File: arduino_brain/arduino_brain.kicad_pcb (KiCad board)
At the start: 2 copper layers, 624 parts, among them J1 Conn_01x08_Male, J2 Conn_01x10_Male, J3 Conn_01x08_Male, J4 Conn_01x06_Male, Q1 2N3904, Q10 2N3904, Q11 2N3906, Q12 STP36NF06L, Q2 TIP120, Q3 2N3904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

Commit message: Updated PCB
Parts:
- added R51: CFR16-10k, Resistor_THT:R_Axial_DIN0204_L3.6mm_D1.6mm_P2.54mm_Vertical, F.Cu at (10.2, -15.2)
- added U2: CRE1S2412SC, Converter_DCDC:Converter_DCDC_muRata_CRE1xxxxxxSC_THT, F.Cu at (0.00, -15.2)
- moved R20 48.2 mm to (20.3, 40.6), turned to 0 degrees
- moved R17 45.0 mm to (20.3, 43.2), turned to 0 degrees
- moved R10 10.5 mm to (33.0, 83.8)
- moved R14 10.5 mm to (35.6, 83.8)
- moved R6 5.08 mm to (27.9, 73.7)
- moved R4 3.59 mm to (30.5, 73.7), turned to 0 degrees
- moved R5 2.54 mm to (27.9, 71.1)
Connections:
- J3 pad 6: COMMODO_GND -> Net-(A1-Pad6)
- R17 pad 1: A1_A2 -> A1_D1
- R20 pad 1: A1_A3 -> A1_D0
- R4 pad 2: A1_D0 -> A1_A2

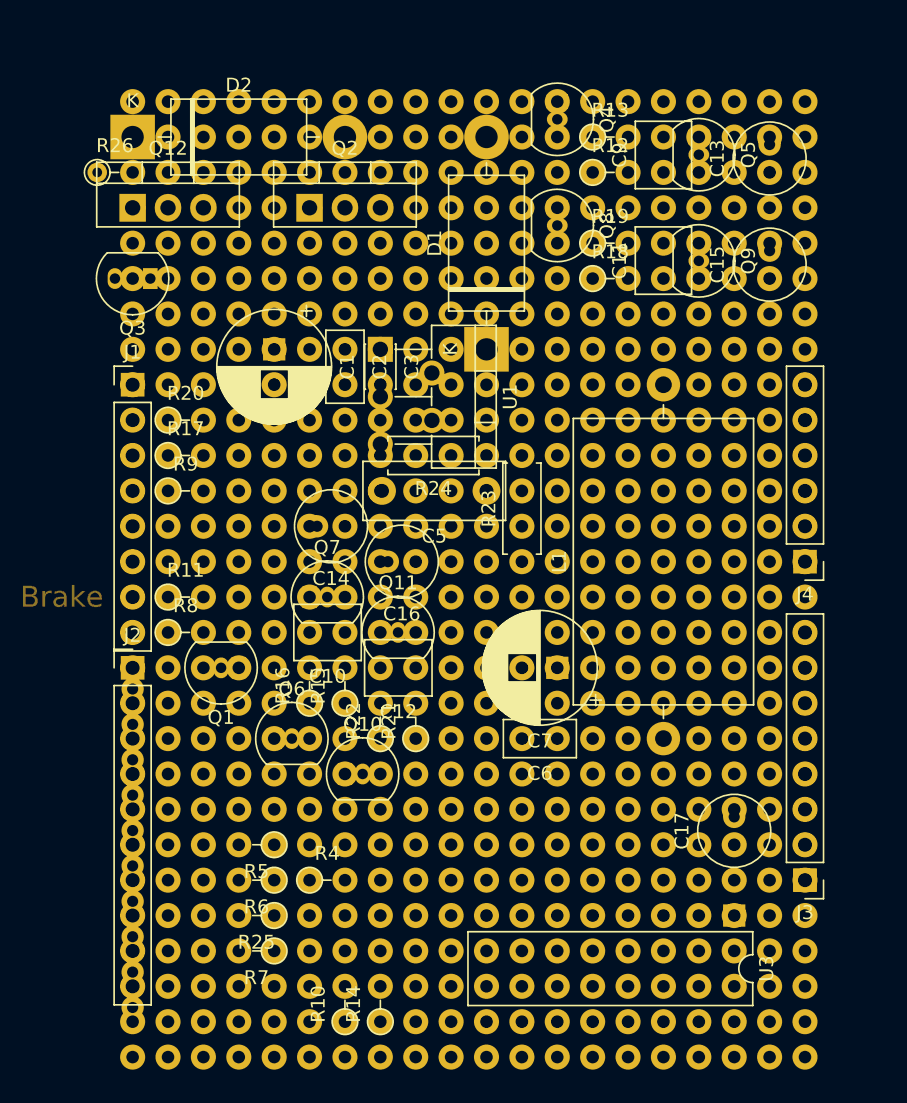
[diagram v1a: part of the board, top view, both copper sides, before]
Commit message: Started routes on PCzb, locking components already placed
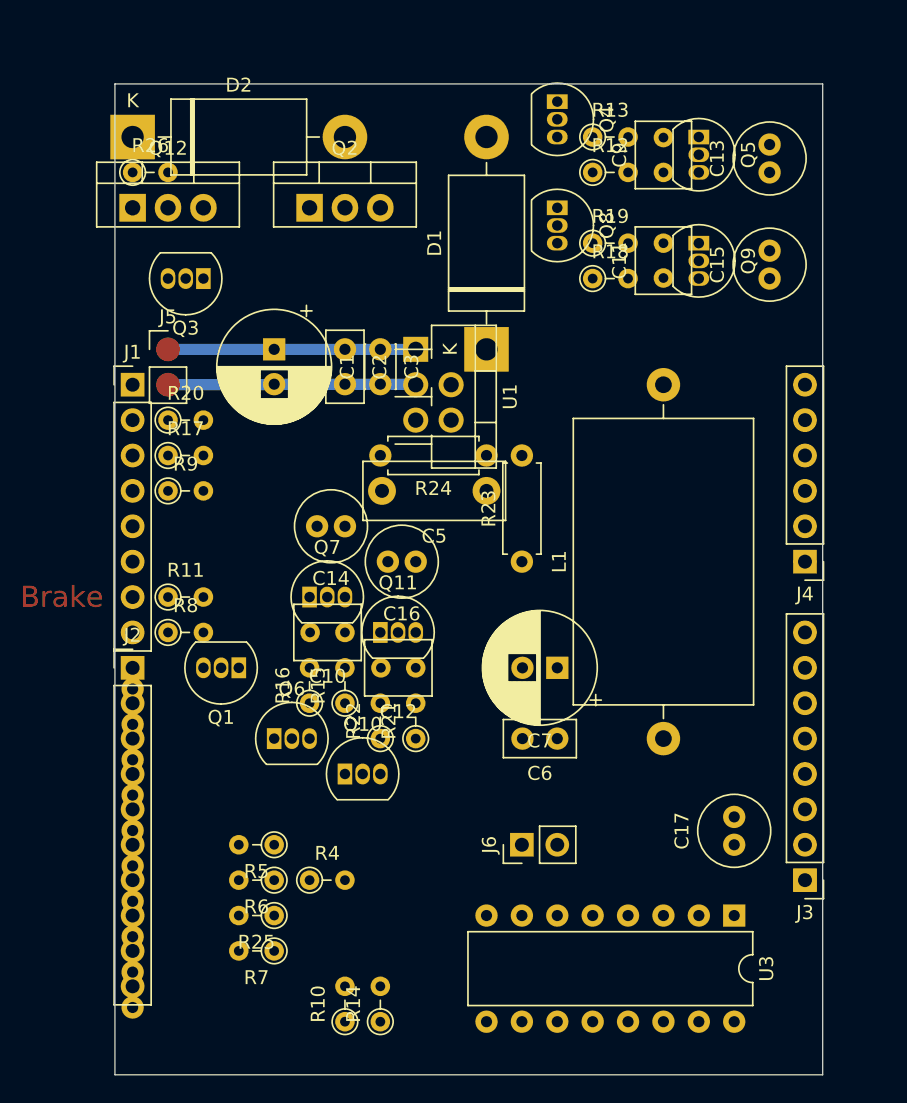
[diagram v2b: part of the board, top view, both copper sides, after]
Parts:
- removed REF** (x560): Pin_D0.9mm_L10.0mm_W2.4mm_FlatFork, Connector_Pin:Pin_D0.9mm_L10.0mm_W2.4mm_FlatFork
- added J5: 12V cable from regulator, Connector_PinHeader_2.54mm:PinHeader_1x02_P2.54mm_Vertical, F.Cu at (20.3, 35.6)
- added J6: 7.5V cables x2 to Arduino power jacks, Connector_PinHeader_2.54mm:PinHeader_1x02_P2.54mm_Vertical, F.Cu at (45.7, 71.1)
- moved Q3 3.81 mm to (22.9, 30.5)
- moved R26 2.54 mm to (17.8, 22.9)
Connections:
- A1 pad 6: Net-(A1-Pad6) -> COMMODO_GND
- J3 pad 6: Net-(A1-Pad6) -> COMMODO_GND
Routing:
- net COMMODO_GND: track 0.00 -> 17.8 mm
- net BEAM_+12V: track 0.00 -> 17.8 mm
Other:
- board outline added: 50.8 x 71.1 mm
- net class Rustic added: clearance 0.35, trace_width 0.8, via_dia 1.91, via_drill 0.4

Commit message: Finsihed solder routes on PCB
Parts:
- moved C8 88.0 mm to (48.3, 66.0), turned to 180 degrees
- moved L1 25.4 mm to (55.9, 38.1), turned to 270 degrees
- moved C15 2.54 mm to (63.5, 33.0)
- moved C13 2.54 mm to (63.5, 25.4)
- moved Q3 2.54 mm to (22.9, 27.9)
- moved R17 2.54 mm to (20.3, 45.7)
- moved R20 2.54 mm to (20.3, 43.2)
- moved R9 2.54 mm to (20.3, 48.3)
- moved Q1 1.27 mm to (24.1, 58.4)
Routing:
- net COMMODO_GND: track 17.8 -> 226.6 mm, vias 0 -> 8
- net BEAM_+12V: track 17.8 -> 152.6 mm, vias 0 -> 1
- net +5V: track 0.00 -> 50.4 mm
- net +7.5V: track 0.00 -> 45.6 mm, vias 0 -> 2
- net Net-(D1-Pad1): track 0.00 -> 15.2 mm, vias 0 -> 2
- net +3V3: track 0.00 -> 12.4 mm
- net INDICATOR_L_+12V: track 0.00 -> 7.62 mm
- net Net-(C5-Pad1): track 0.00 -> 7.62 mm
- net A1_D1: track 0.00 -> 6.31 mm
- net TAILLIGHT_TAILLIGHT: track 0.00 -> 6.13 mm
- net A1_D0: track 0.00 -> 6.13 mm
- net Net-(Q10-Pad3): track 0.00 -> 5.08 mm
- net Net-(Q6-Pad3): track 0.00 -> 5.08 mm
- net Net-(Q12-Pad1): track 0.00 -> 5.08 mm
- net TAILLIGHT_BRAKE: track 0.00 -> 5.08 mm
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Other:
- copper layers 2 -> 4

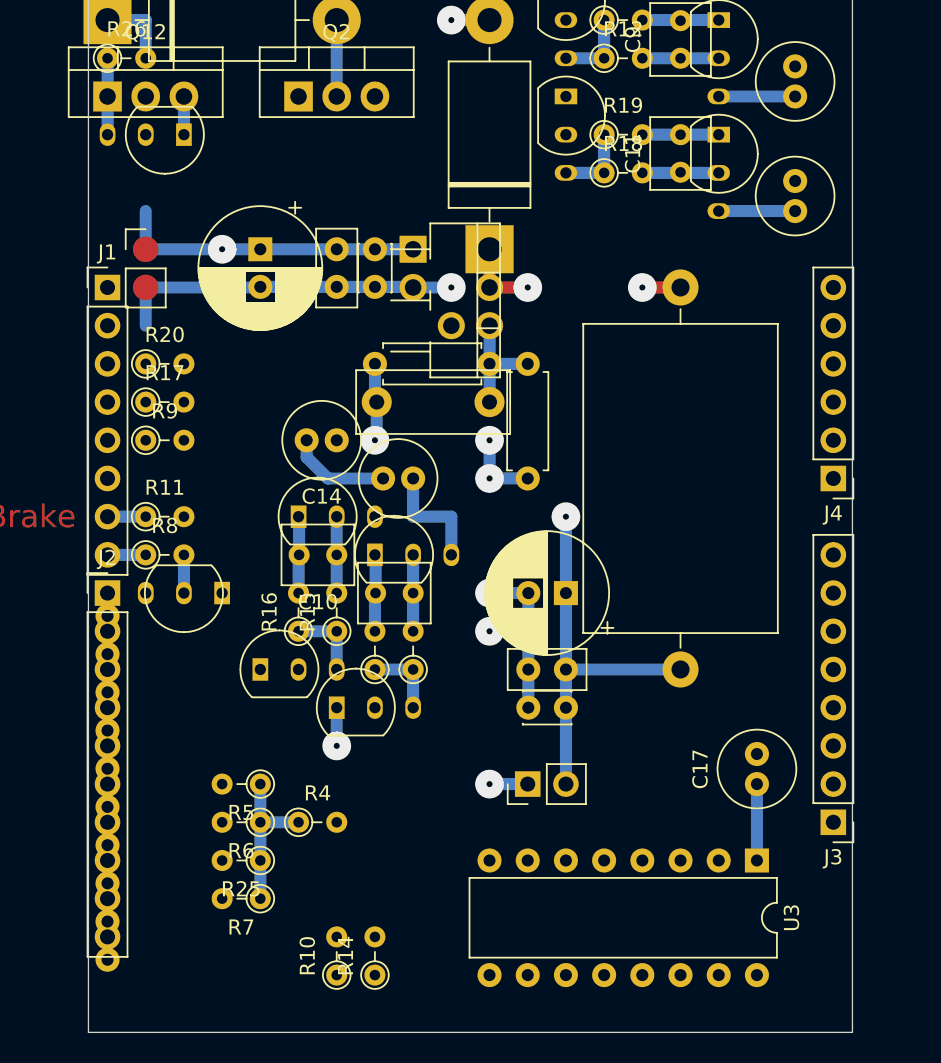
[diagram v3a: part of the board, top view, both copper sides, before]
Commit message: almost finished the layout of passives
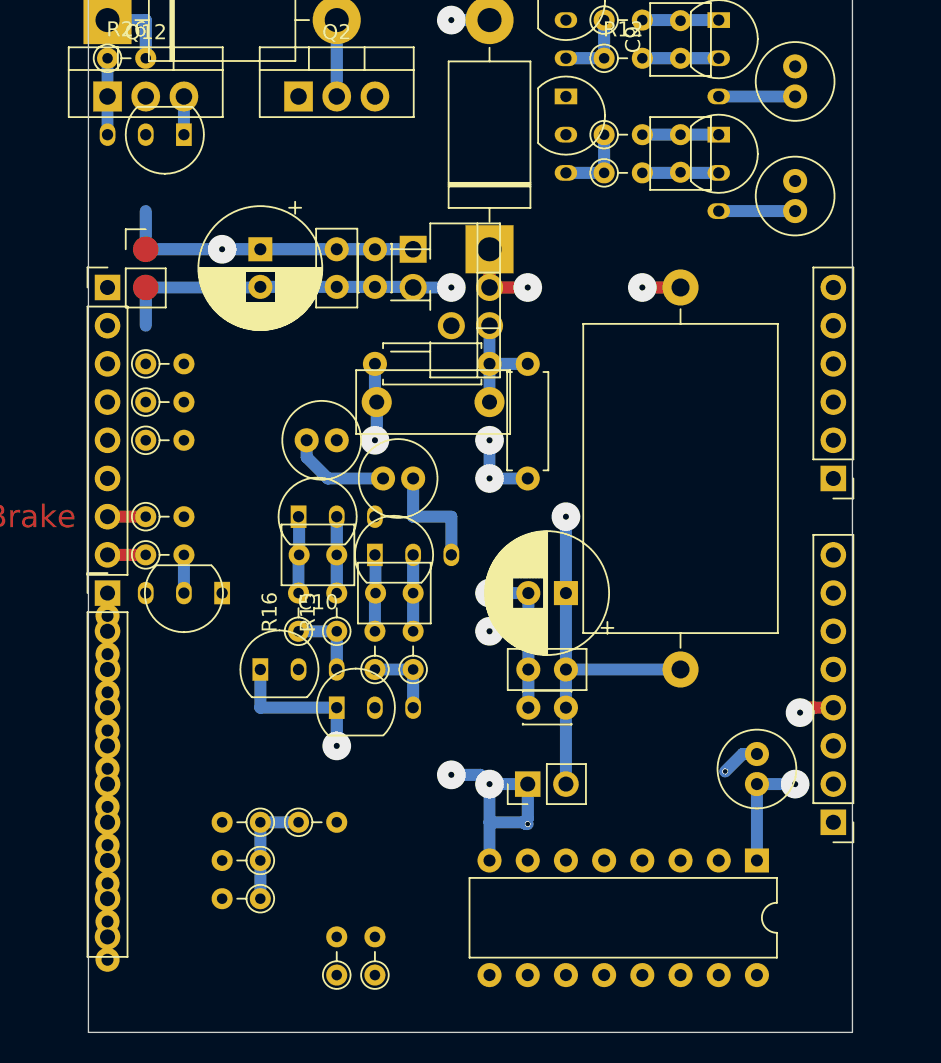
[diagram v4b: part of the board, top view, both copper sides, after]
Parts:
- removed R5: CFR16-10k, Resistor_THT:R_Axial_DIN0204_L3.6mm_D1.6mm_P2.54mm_Vertical
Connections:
- A1 pad 1: Net-(A1-Pad1) -> COMMODO_GND
- A1 pad 29: Net-(A1-Pad1) -> COMMODO_GND
- A2 pad 10: Net-(A2-Pad10) -> (no net)
- A2 pad 11: Net-(A2-Pad11) -> (no net)
- A2 pad 12: Net-(A2-Pad12) -> (no net)
- A2 pad 15: SIM808_D0 -> (no net)
- A2 pad 16: SIM808_D1 -> (no net)
- A2 pad 17: A2_D2 -> (no net)
- A2 pad 18: BUZZER+ -> (no net)
- A2 pad 19: BLUEFRUIT_RST -> (no net)
- A2 pad 2: Net-(A2-Pad2) -> (no net)
- A2 pad 22: BLUEFRUIT_IRQ -> (no net)
- A2 pad 23: BLUEFRUIT_CS -> (no net)
- A2 pad 24: Net-(A2-Pad24) -> (no net)
- A2 pad 25: Net-(A2-Pad25) -> (no net)
- A2 pad 26: ARDUINO_ICSP_3 -> (no net)
- A2 pad 27: ARDUINO_ICSP_1 -> (no net)
- A2 pad 29: Net-(A2-Pad29) -> (no net)
- A2 pad 3: Net-(A2-Pad3) -> (no net)
- A2 pad 30: Net-(A2-Pad30) -> (no net)
- A2 pad 31: 9DoF_SDA -> (no net)
- A2 pad 32: 9DoF_SCL -> (no net)
- A2 pad 4: Net-(A2-Pad4) -> (no net)
- A2 pad 5: Net-(A2-Pad5) -> (no net)
- A2 pad 6: Net-(A2-Pad6) -> (no net)
- A2 pad 9: A2_A0 -> (no net)
- J2 pad 7: Net-(A1-Pad1) -> COMMODO_GND
- J3 pad 1: Net-(J3-Pad1) -> (no net)
- Q1 pad 1: CA_ECO_MODE_GND -> (no net)
- Q1 pad 3: CA_ECO_MODE_HI -> (no net)
- Q12 pad 2: BEAM_GND -> (no net)
- R51 pad 2: COMMODO_RIGHT -> (no net)
- U1 pad 5: Net-(U1-Pad5) -> (no net)
- U2 pad 2: +BATT -> (no net)
- U3 pad 10: Net-(U3-Pad10) -> (no net)
- U3 pad 11: Net-(U3-Pad11) -> (no net)
- U3 pad 12: Net-(U3-Pad12) -> (no net)
- U3 pad 13: Net-(U3-Pad13) -> (no net)
- U3 pad 15: Net-(U3-Pad15) -> (no net)
- U3 pad 16: Net-(U3-Pad16) -> (no net)
- U3 pad 2: Net-(U3-Pad2) -> (no net)
- U3 pad 4: Net-(U3-Pad4) -> (no net)
- U3 pad 6: Net-(U3-Pad6) -> (no net)
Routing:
- net COMMODO_GND: track 226.6 -> 257.5 mm, vias 8 -> 11
- net +3V3: track 12.4 -> 16.4 mm, vias 0 -> 2
- net +5V: track 50.4 -> 47.9 mm
